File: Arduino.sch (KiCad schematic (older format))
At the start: 23 parts

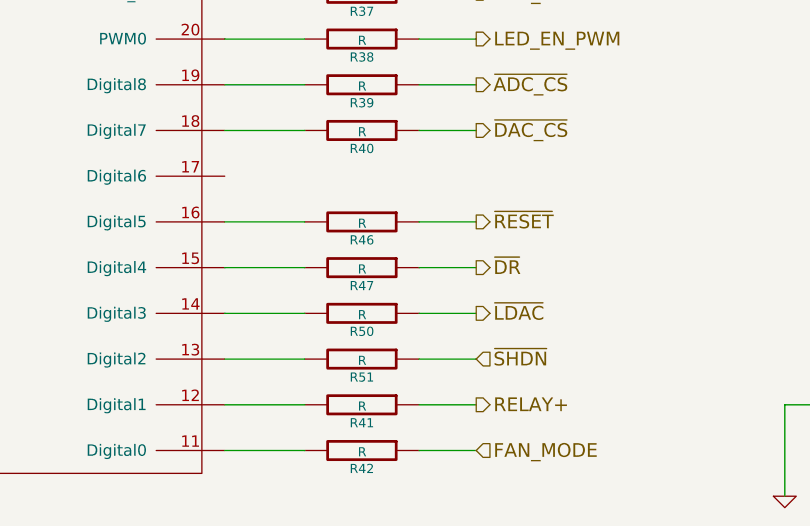
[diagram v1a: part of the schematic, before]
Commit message: Layout Work Session 12
Pulled from CE.

Session 11 missed due to corrupted pcb file pulled from CE
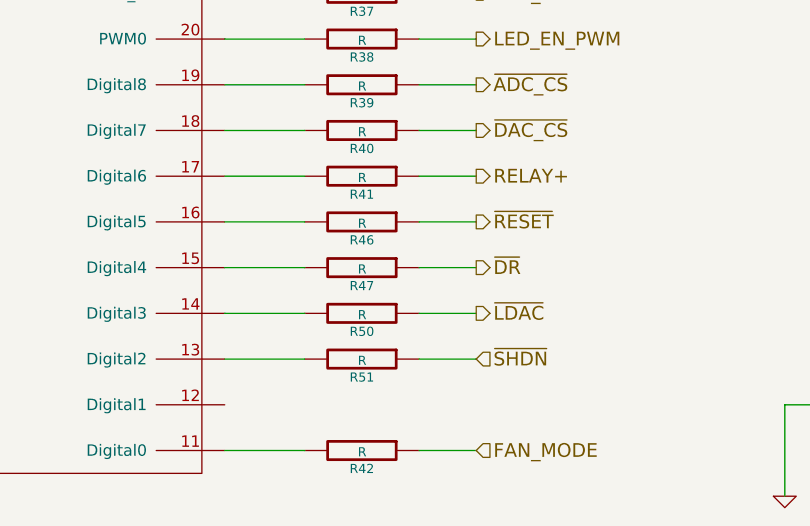
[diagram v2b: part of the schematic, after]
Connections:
- net at R41.2: now also ARD1.17 (Digital6); no longer ARD1.12 (Digital1)
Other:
- moved on the sheet: R41
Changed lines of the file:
@@
-EESchema Schematic File Version 2
+EESchema Schematic File Version 2  date 11/21/2013 11:46:41 PM
 LIBS:power
 LIBS:device
@@
 LIBS:BenchBuddy
 LIBS:BenchBuddy-cache
-EELAYER 24 0
+EELAYER 27 0
 EELAYER END
 $Descr A4 11693 8268
@@
 Sheet 8 9
 Title ""
-Date "13 nov 2013"
+Date "22 nov 2013"
 Rev ""
 Comp ""
@@
 Comment4 ""
 $EndDescr
-Text HLabel 7150 5700 2    60   Output ~ 0
+Text HLabel 7150 4700 2    60   Output ~ 0
 RELAY+
 Text HLabel 9300 5700 2    60   Output ~ 0
@@
 L R R41
 U 1 1 52400F79
-P 6650 5700
-F 0 "R41" V 6730 5700 40  0000 C CNN
-F 1 "R" V 6657 5701 40  0000 C CNN
-F 2 "~" V 6580 5700 30  0000 C CNN
-F 3 "~" H 6650 5700 30  0000 C CNN
-	1    6650 5700
-	0    1    1    0
-$EndComp
-Wire Wire Line
-	7150 5700 6900 5700
-Wire Wire Line
-	6400 5700 6050 5700
+P 6650 4700
+F 0 "R41" V 6730 4700 40  0000 C CNN
+F 1 "R" V 6657 4701 40  0000 C CNN
+F 2 "~" V 6580 4700 30  0000 C CNN
+F 3 "~" H 6650 4700 30  0000 C CNN
+	1    6650 4700
+	0    1    1    0
+$EndComp
+Wire Wire Line
+	7150 4700 6900 4700
 Wire Wire Line
 	8500 5700 8500 6100
 $Comp
-L GND #PWR040
+L GND #PWR039
 U 1 1 524020EC
 P 8500 6100
-F 0 "#PWR040" H 8500 6100 30  0001 C CNN
+F 0 "#PWR039" H 8500 6100 30  0001 C CNN
 F 1 "GND" H 8500 6030 30  0001 C CNN
 F 2 "~" H 8500 6100 60  0000 C CNN
@@
 	3350 4350 3850 4350
 $Comp
-L +12P #PWR041
+L +12P #PWR040
 U 1 1 5243CFCD
 P 1200 4050
-F 0 "#PWR041" H 1200 4020 30  0001 C CNN
+F 0 "#PWR040" H 1200 4020 30  0001 C CNN
 F 1 "+12P" H 1200 4150 30  0000 C CNN
 F 2 "~" H 1200 4050 60  0000 C CNN
@@
 	3350 3750 3850 3750
 $Comp
-L +5V #PWR042
+L +5V #PWR041
 U 1 1 5245176C
 P 1200 3500
-F 0 "#PWR042" H 1200 3590 20  0001 C CNN
+F 0 "#PWR041" H 1200 3590 20  0001 C CNN
 F 1 "+5V" H 1200 3590 30  0000 C CNN
 F 2 "~" H 1200 3500 60  0000 C CNN
@@
 	2100 3950 2100 4150
 $Comp
-L GND #PWR043
+L GND #PWR042
 U 1 1 5245181B
 P 2100 4150
-F 0 "#PWR043" H 2100 4150 30  0001 C CNN
+F 0 "#PWR042" H 2100 4150 30  0001 C CNN
 F 1 "GND" H 2100 4080 30  0001 C CNN
 F 2 "~" H 2100 4150 60  0000 C CNN
@@
 Wire Wire Line
 	6900 5300 7150 5300
+Wire Wire Line
+	6400 4700 6050 4700
 $EndSCHEMATC
